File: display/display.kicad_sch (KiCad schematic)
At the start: 19 parts, among them J1 DIN41612_03x32_ABC

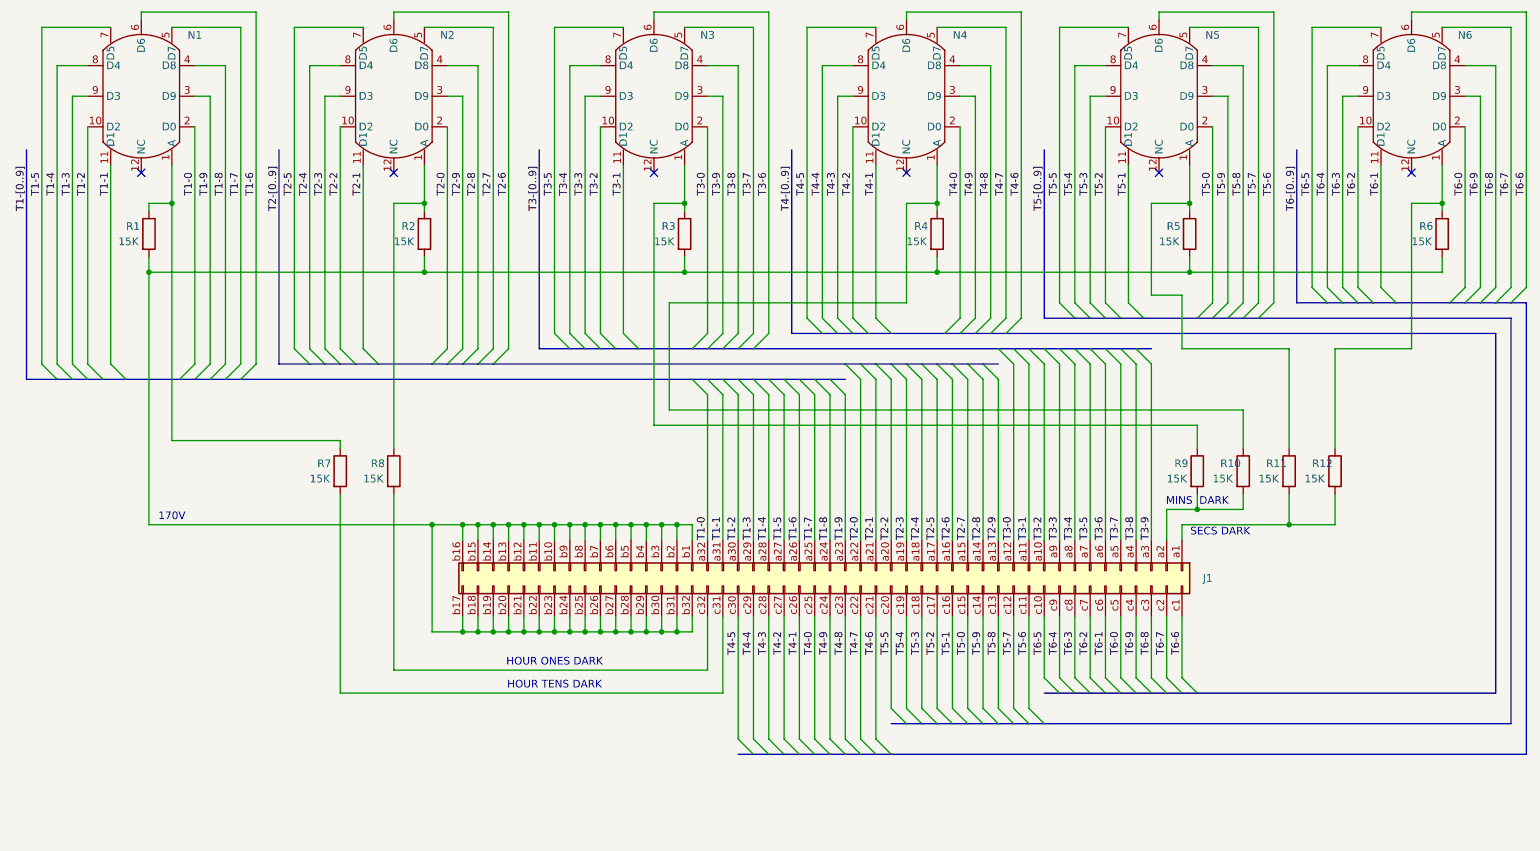
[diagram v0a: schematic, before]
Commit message: Schematic corrected and display board is partially routed
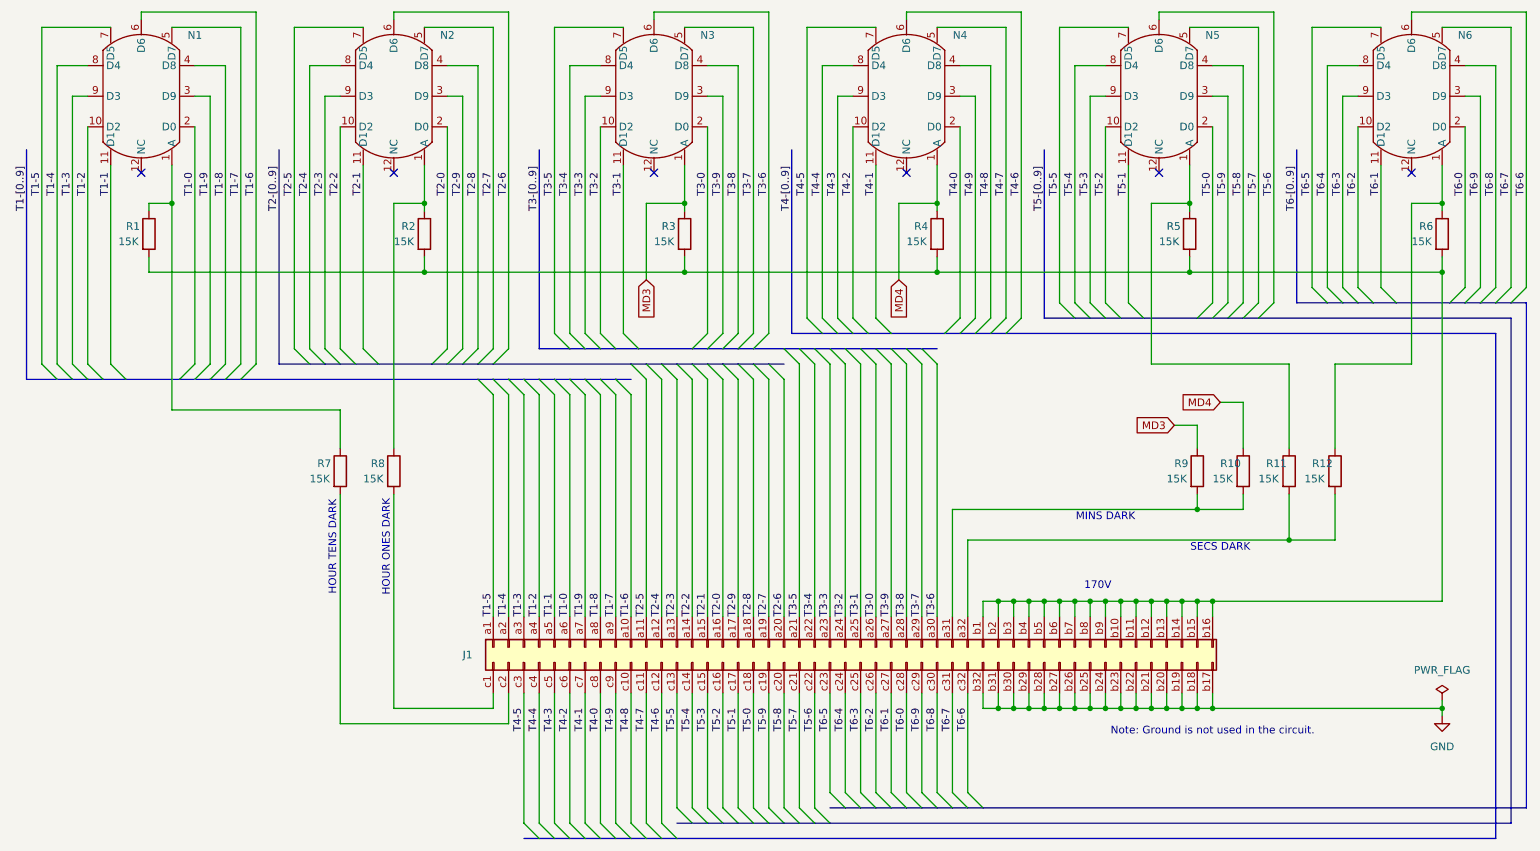
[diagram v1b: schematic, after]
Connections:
- net T1-0: now also J1.a6 (Pin_a6); no longer J1.a32 (Pin_a32)
- net T1-1: now also J1.a5 (Pin_a5); no longer J1.a31 (Pin_a31)
- net T1-2: now also J1.a4 (Pin_a4); no longer J1.a30 (Pin_a30)
- net T1-3: now also J1.a3 (Pin_a3); no longer J1.a29 (Pin_a29)
- net T1-4: now also J1.a2 (Pin_a2); no longer J1.a28 (Pin_a28)
- net T1-5: now also J1.a1 (Pin_a1); no longer J1.a27 (Pin_a27)
- net T1-6: now also J1.a10 (Pin_a10); no longer J1.a26 (Pin_a26)
- net T1-7: now also J1.a9 (Pin_a9); no longer J1.a25 (Pin_a25)
- net T1-8: now also J1.a8 (Pin_a8); no longer J1.a24 (Pin_a24)
- net T1-9: now also J1.a7 (Pin_a7); no longer J1.a23 (Pin_a23)
- net T2-0: now also J1.a16 (Pin_a16); no longer J1.a22 (Pin_a22)
- net T2-1: now also J1.a15 (Pin_a15); no longer J1.a21 (Pin_a21)
- net T2-2: now also J1.a14 (Pin_a14); no longer J1.a20 (Pin_a20)
- net T2-3: now also J1.a13 (Pin_a13); no longer J1.a19 (Pin_a19)
- net T2-4: now also J1.a12 (Pin_a12); no longer J1.a18 (Pin_a18)
- net T2-5: now also J1.a11 (Pin_a11); no longer J1.a17 (Pin_a17)
- net T2-6: now also J1.a20 (Pin_a20); no longer J1.a16 (Pin_a16)
- net T2-7: now also J1.a19 (Pin_a19); no longer J1.a15 (Pin_a15)
- net T2-8: now also J1.a18 (Pin_a18); no longer J1.a14 (Pin_a14)
- net T2-9: now also J1.a17 (Pin_a17); no longer J1.a13 (Pin_a13)
- net T3-0: now also J1.a26 (Pin_a26); no longer J1.a12 (Pin_a12)
- net T3-1: now also J1.a25 (Pin_a25); no longer J1.a11 (Pin_a11)
- net T3-2: now also J1.a24 (Pin_a24); no longer J1.a10 (Pin_a10)
- net T3-3: now also J1.a23 (Pin_a23); no longer J1.a9 (Pin_a9)
- net T3-4: now also J1.a22 (Pin_a22); no longer J1.a8 (Pin_a8)
- net T3-5: now also J1.a21 (Pin_a21); no longer J1.a7 (Pin_a7)
- net T3-6: now also J1.a30 (Pin_a30); no longer J1.a6 (Pin_a6)
- net T3-7: now also J1.a29 (Pin_a29); no longer J1.a5 (Pin_a5)
- net T3-8: now also J1.a28 (Pin_a28); no longer J1.a4 (Pin_a4)
- net T3-9: now also J1.a27 (Pin_a27); no longer J1.a3 (Pin_a3)
- net T4-0: now also J1.c8 (Pin_c8); no longer J1.c25 (Pin_c25)
- net T4-1: now also J1.c7 (Pin_c7); no longer J1.c26 (Pin_c26)
- net T4-2: now also J1.c6 (Pin_c6); no longer J1.c27 (Pin_c27)
- net T4-3: now also J1.c5 (Pin_c5); no longer J1.c28 (Pin_c28)
- net T4-4: now also J1.c4 (Pin_c4); no longer J1.c29 (Pin_c29)
- net T4-5: now also J1.c3 (Pin_c3); no longer J1.c30 (Pin_c30)
- net T4-6: now also J1.c12 (Pin_c12); no longer J1.c21 (Pin_c21)
- net T4-7: now also J1.c11 (Pin_c11); no longer J1.c22 (Pin_c22)
- net T4-8: now also J1.c10 (Pin_c10); no longer J1.c23 (Pin_c23)
- net T4-9: now also J1.c9 (Pin_c9); no longer J1.c24 (Pin_c24)
- net T5-0: now also J1.c18 (Pin_c18); no longer J1.c15 (Pin_c15)
- net T5-1: now also J1.c17 (Pin_c17); no longer J1.c16 (Pin_c16)
- net T5-2: now also J1.c16 (Pin_c16); no longer J1.c17 (Pin_c17)
- net T5-3: now also J1.c15 (Pin_c15); no longer J1.c18 (Pin_c18)
- net T5-4: now also J1.c14 (Pin_c14); no longer J1.c19 (Pin_c19)
- net T5-5: now also J1.c13 (Pin_c13); no longer J1.c20 (Pin_c20)
- net T5-6: now also J1.c22 (Pin_c22); no longer J1.c11 (Pin_c11)
- net T5-7: now also J1.c21 (Pin_c21); no longer J1.c12 (Pin_c12)
- net T5-8: now also J1.c20 (Pin_c20); no longer J1.c13 (Pin_c13)
- net T5-9: now also J1.c19 (Pin_c19); no longer J1.c14 (Pin_c14)
- net T6-0: now also J1.c28 (Pin_c28); no longer J1.c5 (Pin_c5)
- net T6-1: now also J1.c27 (Pin_c27); no longer J1.c6 (Pin_c6)
- net T6-2: now also J1.c26 (Pin_c26); no longer J1.c7 (Pin_c7)
- net T6-3: now also J1.c25 (Pin_c25); no longer J1.c8 (Pin_c8)
- net T6-4: now also J1.c24 (Pin_c24); no longer J1.c9 (Pin_c9)
- net T6-5: now also J1.c23 (Pin_c23); no longer J1.c10 (Pin_c10)
- net T6-6: now also J1.c32 (Pin_c32); no longer J1.c1 (Pin_c1)
- net T6-7: now also J1.c31 (Pin_c31); no longer J1.c2 (Pin_c2)
- net T6-8: now also J1.c30 (Pin_c30); no longer J1.c3 (Pin_c3)
- net T6-9: now also J1.c29 (Pin_c29); no longer J1.c4 (Pin_c4)
- net at R8.2: now also J1.c1 (Pin_c1); no longer J1.c32 (Pin_c32)
- net at R11.2, R12.2: now also J1.a32 (Pin_a32); no longer J1.a1 (Pin_a1)
- net MD4: now reaches N4.1 (A), R10.1, R4.1
- net at J1.b1 (Pin_b1), J1.b10 (Pin_b10), J1.b11 (Pin_b11)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: no longer J1.b17 (Pin_b17), J1.b18 (Pin_b18), J1.b19 (Pin_b19), J1.b20 (Pin_b20), J1.b21 (Pin_b21), J1.b22 (Pin_b22), J1.b23 (Pin_b23), J1.b24 (Pin_b24), J1.b25 (Pin_b25), J1.b26 (Pin_b26), J1.b27 (Pin_b27), J1.b28 (Pin_b28), J1.b29 (Pin_b29), J1.b30 (Pin_b30), J1.b31 (Pin_b31), J1.b32 (Pin_b32)
- net at R7.2: now also J1.c2 (Pin_c2); no longer J1.c31 (Pin_c31)
- net MD3: now reaches N3.1 (A), R3.1, R9.1
- net at R10.2, R9.2: now also J1.a31 (Pin_a31); no longer J1.a2 (Pin_a2)
- new net GND: J1.b17 (Pin_b17), J1.b18 (Pin_b18), J1.b19 (Pin_b19), J1.b20 (Pin_b20), J1.b21 (Pin_b21), J1.b22 (Pin_b22), J1.b23 (Pin_b23), J1.b24 (Pin_b24), J1.b25 (Pin_b25), J1.b26 (Pin_b26), J1.b27 (Pin_b27), J1.b28 (Pin_b28), J1.b29 (Pin_b29), J1.b30 (Pin_b30), J1.b31 (Pin_b31), J1.b32 (Pin_b32)
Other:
- note added: "Note: Ground is not used in the circuit."
- moved on the sheet: J1
